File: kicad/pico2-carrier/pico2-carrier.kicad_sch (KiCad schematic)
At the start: 21 parts, among them IC1 TFBS4711-TT1, IC2 M95512-DRMN8TP_K, IC3 IS25WP128F-JBLE, J1 Conn_01x07_Pin, J2 DBG, J3 Ext_Pwr_Rail, SW1 BUT_L, SW2 BUT_M, SW3 BUT_R, U1 Pico 2, U2 BMA400

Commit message: hw: screen updates
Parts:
- J1: symbol Connector:Conn_01x07_Pin -> Connector:Conn_01x08_Pin
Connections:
- net GND: now also J1.8 (Pin_8); no longer J1.7 (Pin_7)
- net ~{SCREEN_RST}: now reaches U1.29 (GPIO22)
- net ~{SCREEN_RST}: now also J1.7 (Pin_7)
- net SCREEN_PWR_EN: now reaches U1.32 (GPIO27_ADC1)
- no-connect marks 9 -> 8
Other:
- note added: "Software reset might be sufficient"
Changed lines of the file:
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@@
 	)
 	(no_connect
-		(at 128.27 135.89)
-	)
-	(no_connect
 		(at 121.92 110.49)
 	)
@@
 	(wire
 		(pts
-			(xy 102.87 76.2) (xy 116.84 76.2)
+			(xy 119.38 128.27) (xy 135.89 128.27)
 		)
 		(stroke
@@
 	(wire
 		(pts
-			(xy 119.38 125.73) (xy 138.43 125.73)
+			(xy 119.38 125.73) (xy 148.59 125.73)
 		)
 		(stroke
@@
 	(wire
 		(pts
+			(xy 102.87 78.74) (xy 116.84 78.74)
+		)
+		(stroke
+			(width 0)
+			(type default)
+		)
+	)
+	(wire
+		(pts
 			(xy 119.38 113.03) (xy 137.16 113.03)
 		)
@@
 	(wire
 		(pts
-			(xy 119.38 135.89) (xy 128.27 135.89)
+			(xy 119.38 135.89) (xy 134.62 135.89)
 		)
 		(stroke
@@
 	(wire
 		(pts
+			(xy 102.87 76.2) (xy 119.38 76.2)
+		)
+		(stroke
+			(width 0)
+			(type default)
+		)
+	)
+	(wire
+		(pts
 			(xy 127 40.64) (xy 127 43.18)
 		)
@@
 		)
 	)
+	(text "Software reset might be sufficient"
+		(exclude_from_sim no)
+		(at 151.892 135.128 0)
+		(effects
+			(font
+				(size 1.27 1.27)
+			)
+		)
+	)
 	(text "1.7V - 5.5V at normal temperatures"
 		(exclude_from_sim no)
@@
 		)
 	)
+	(label "~{SCREEN_RST}"
+		(at 119.38 76.2 180)
+		(fields_autoplaced yes)
+		(effects
+			(font
+				(size 1.27 1.27)
+			)
+			(justify right bottom)
+		)
+	)
 	(label "BUT_R"
 		(at 127 21.59 0)
@@
 		)
 	)
+	(label "~{SCREEN_RST}"
+		(at 134.62 135.89 180)
+		(fields_autoplaced yes)
+		(effects
+			(font
+				(size 1.27 1.27)
+			)
+			(justify right bottom)
+		)
+	)
 	(label "BUT_L"
 		(at 66.04 140.97 0)
@@
 		)
 	)
+	(label "SCREEN_PWR_EN"
+		(at 135.89 128.27 180)
+		(fields_autoplaced yes)
+		(effects
+			(font
+				(size 1.27 1.27)
+			)
+			(justify right bottom)
+		)
+	)
 	(label "~{SCREEN_CSB}"
 		(at 119.38 60.96 180)
@@
 	)
 	(symbol
-		(lib_name "GND_1")
-		(lib_id "power:GND")
-		(at 116.84 76.2 0)
-		(unit 1)
-		(exclude_from_sim no)
-		(in_bom yes)
-		(on_board yes)
-		(dnp no)
-		(fields_autoplaced yes)
-		(property "Reference" "#PWR09"
-			(at 116.84 82.55 0)
-			(effects
-				(font
-					(size 1.27 1.27)
-				)
-				(hide yes)
-			)
-		)
-		(property "Value" "GND"
-			(at 116.84 81.28 0)
-			(effects
-				(font
-					(size 1.27 1.27)
-				)
-			)
-		)
-		(property "Footprint" ""
-			(at 116.84 76.2 0)
-			(effects
-				(font
-					(size 1.27 1.27)
-				)
-				(hide yes)
-			)
-		)
-		(property "Datasheet" ""
-			(at 116.84 76.2 0)
-			(effects
-				(font
-					(size 1.27 1.27)
-				)
-				(hide yes)
-			)
-		)
-		(property "Description" "Power symbol creates a global label with name \"GND\" , ground"
-			(at 116.84 76.2 0)
-			(effects
-				(font
-					(size 1.27 1.27)
-				)
-				(hide yes)
-			)
-		)
-		(pin "1"
-		)
-		(instances
-			(project "pico2-carrier"
-				(path "/4204b4ad-0ae5-4a8a-a079-fb4cf2b0ed9e"
-					(reference "#PWR09")
-					(unit 1)
-				)
-			)
-		)
-	)
-	(symbol
 		(lib_id "power:+3.3V")
 		(at 280.67 52.07 0)
@@
 	)
 	(symbol
-		(lib_id "Connector:Conn_01x07_Pin")
+		(lib_id "Connector:Conn_01x08_Pin")
 		(at 97.79 68.58 0)
 		(unit 1)
@@
 			)
 		)
-		(property "Description" "Generic connector, single row, 01x07, script generated"
+		(property "Description" "Generic connector, single row, 01x08, script generated"
 			(at 97.79 68.58 0)
 			(effects
@@
 		(pin "1"
 		)
+		(pin "8"
+		)
 		(instances
 			(project ""
@@
 		(lib_name "GND_1")
 		(lib_id "power:GND")
-		(at 138.43 125.73 0)
+		(at 148.59 125.73 0)
 		(unit 1)
 		(exclude_from_sim no)
@@
 		(fields_autoplaced yes)
 		(property "Reference" "#PWR027"
-			(at 138.43 132.08 0)
+			(at 148.59 132.08 0)
 			(effects
 				(font
@@
 		)
 		(property "Value" "GND"
-			(at 138.43 130.81 0)
+			(at 148.59 130.81 0)
 			(effects
 				(font
@@
 		)
 		(property "Footprint" ""
-			(at 138.43 125.73 0)
+			(at 148.59 125.73 0)
 			(effects
 				(font
@@
 		)
 		(property "Datasheet" ""
-			(at 138.43 125.73 0)
+			(at 148.59 125.73 0)
 			(effects
 				(font
@@
 		)
 		(property "Description" "Power symbol creates a global label with name \"GND\" , ground"
-			(at 138.43 125.73 0)
+			(at 148.59 125.73 0)
 			(effects
 				(font
@@
 					(unit 1)
 				)
+			)
+		)
+	)
+	(symbol
+		(lib_name "GND_1")
+		(lib_id "power:GND")
+		(at 116.84 78.74 0)
+		(unit 1)
+		(exclude_from_sim no)
+		(in_bom yes)
+		(on_board yes)
+		(dnp no)
+		(fields_autoplaced yes)
+		(property "Reference" "#PWR09"
+			(at 116.84 85.09 0)
+			(effects
+				(font
+					(size 1.27 1.27)
+				)
+				(hide yes)
+			)
+		)
+		(property "Value" "GND"
+			(at 116.84 83.82 0)
+			(effects
+				(font
+					(size 1.27 1.27)
+				)
+			)
+		)
+		(property "Footprint" ""
+			(at 116.84 78.74 0)
+			(effects
+				(font
+					(size 1.27 1.27)
+				)
+				(hide yes)
+			)
+		)
+		(property "Datasheet" ""
+			(at 116.84 78.74 0)
+			(effects
+				(font
+					(size 1.27 1.27)
+				)
+				(hide yes)
+			)
+		)
+		(property "Description" "Power symbol creates a global label with name \"GND\" , ground"
+			(at 116.84 78.74 0)
+			(effects
+				(font
+					(size 1.27 1.27)
+				)
+				(hide yes)
+			)
+		)
+		(pin "1"
+		)
+		(instances
+			(project "pico2-carrier"
+				(path "/4204b4ad-0ae5-4a8a-a079-fb4cf2b0ed9e"
+					(reference "#PWR09")
+					(unit 1)
+				)

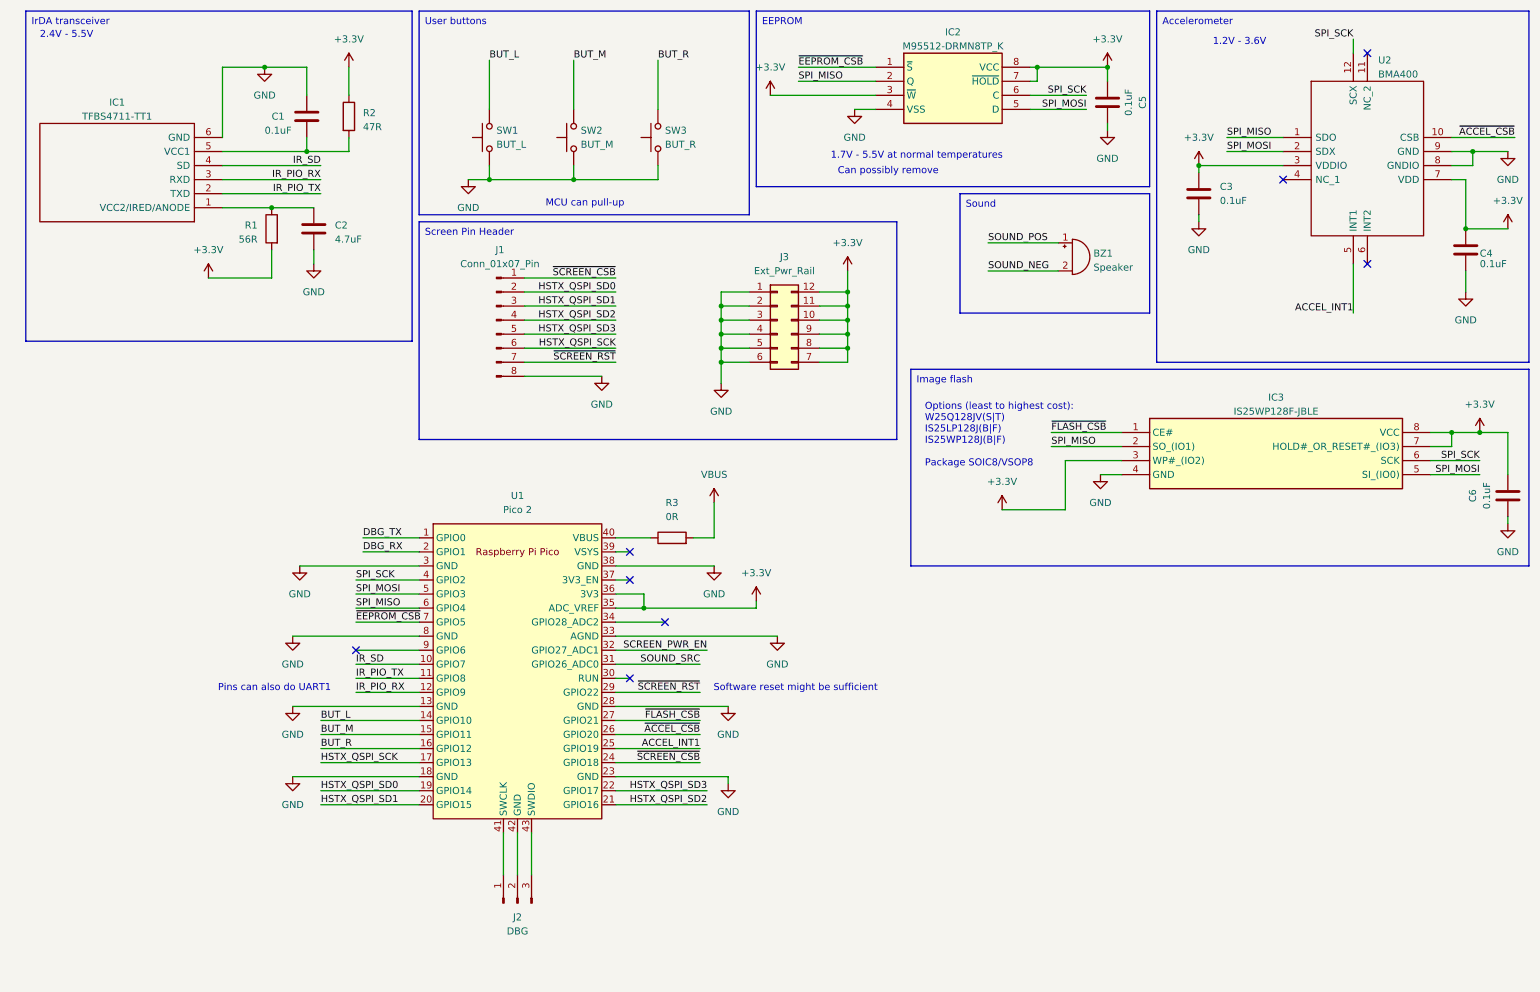
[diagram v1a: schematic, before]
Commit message: hw: update screen stuff
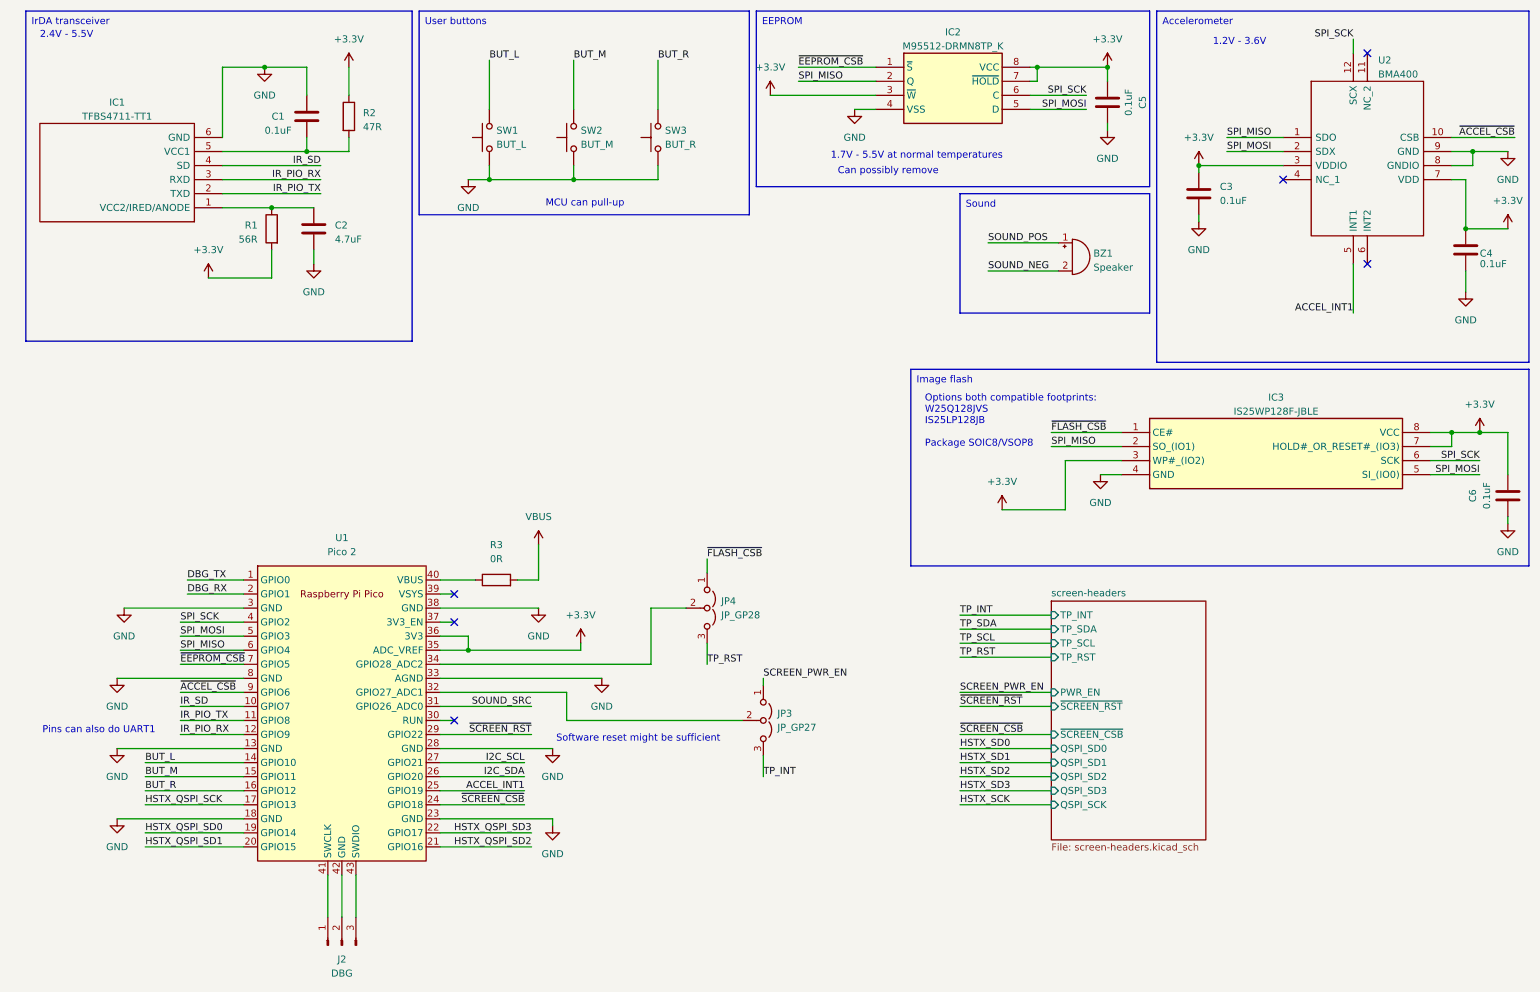
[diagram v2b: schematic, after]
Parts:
- removed J1: Conn_01x07_Pin, symbol Connector:Conn_01x08_Pin
- removed J3: Ext_Pwr_Rail, symbol Connector_Generic:Conn_02x06_Counter_Clockwise
- added JP3: JP_GP27, symbol Jumper:Jumper_3_Open
- added JP4: JP_GP28, symbol Jumper:Jumper_3_Open
- IC1: footprint Samacsys_Parts:TFBS4711TT1 -> SamacsysParts:TFBS4711TT1
- IC2: footprint SOIC127P600X175-8N -> SamacsysParts:SOIC127P600X175-8N
- IC3: footprint SOIC127P790X216-8N -> SamacsysParts:SOIC127P790X216-8N
- J2: footprint (none) -> Connector_PinHeader_2.54mm:PinHeader_1x03_P2.54mm_Vertical
- R3: footprint (none) -> Resistor_SMD:R_0805_2012Metric
- SW1, SW2, SW3: footprint Samacsys_Parts:TL3315NF100Q -> SamacsysParts:TL3315NF100Q
- U2: footprint Samacsys_Parts:BOSCH_LGA-12 -> SamacsysParts:BOSCH_LGA-12
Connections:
- net SCREEN_PWR_EN: now also JP3.1 (A); no longer U1.32 (GPIO27_ADC1)
- net ~{ACCEL_CSB}: now also U1.9 (GPIO6); no longer U1.26 (GPIO20)
- net ~{FLASH_CSB}: now also JP4.1 (A); no longer U1.27 (GPIO21)
- net at U1.34 (GPIO28_ADC2): now also JP4.2 (C)
- new net: JP3.2 (C), U1.32 (GPIO27_ADC1)
- new net I2C_SCL: U1.27 (GPIO21)
- new net I2C_SDA: U1.26 (GPIO20)
- new net TP_INT: JP3.3 (B)
- new net TP_RST: JP4.3 (B)
- no-connect marks 8 -> 6
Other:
- added sheet screen-headers (screen-headers.kicad_sch)
- note added: "Options both compatible footprints: W25Q128JVS IS25LP128JB Package SOIC8/VSOP8"
- note removed: "Options (least to highest cost): W25Q128JV(S|T) IS25LP128J(B|F) IS25WP128J(B|F) Package SOIC8/VSOP8"
- moved on the sheet: J2, R3, U1

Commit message: hw: lots of changes to pico 2 board
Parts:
- removed BZ1: Speaker, Jumper:SolderJumper-2_P1.3mm_Open_Pad1.0x1.5mm, symbol Device:Buzzer
- removed J2: DBG, Connector_PinHeader_2.54mm:PinHeader_1x03_P2.54mm_Vertical, symbol Connector:Conn_01x03_Pin
- removed JP3: JP_GP27, symbol Jumper:Jumper_3_Open
- removed JP4: JP_GP28, symbol Jumper:Jumper_3_Open
- removed R3: 0R, Resistor_SMD:R_0805_2012Metric, symbol Device:R
- removed U2: BMA400, SamacsysParts:BOSCH_LGA-12, symbol SamacSys_Parts:BMA400
- added AC1: BMA400, SamacsysParts:BOSCH_LGA-12, symbol SamacSys_Parts:BMA400
- added H1, H2, H3, H4: MountingHole, MountingHole:MountingHole_2.2mm_M2, symbol Mechanical:MountingHole
- added JP1, JP2: Jumper_2_Open, Connector_PinHeader_2.54mm:PinHeader_1x02_P2.54mm_Vertical, symbol Jumper:Jumper_2_Open
- added JP5: 3V3_CURRENT_SENSE, Connector_PinHeader_2.54mm:PinHeader_1x02_P2.54mm_Vertical, symbol Jumper:Jumper_2_Open
- added R8, R9: 10k, Resistor_SMD:R_0402_1005Metric, symbol Device:R
- added SW4: RUN, Button_Switch_SMD:SW_SPST_Omron_B3FS-101xP, symbol Switch:SW_Push
- SW1, SW2, SW3: footprint SamacsysParts:TL3315NF100Q -> Button_Switch_SMD:SW_SPST_Omron_B3FS-101xP
- renumbered C5 to C3, C3 to C4, C4 to C5
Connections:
- net HSTX_QSPI_SCK is gone; now on net HSTX_SD0: U1.17 (GPIO13)
- net HSTX_QSPI_SD0 is gone; now on net HSTX_SD1: U1.19 (GPIO14)
- net HSTX_QSPI_SD1 is gone; now on net HSTX_SCK: U1.20 (GPIO15)
- net HSTX_QSPI_SD2 is gone; now on net HSTX_SD2: U1.21 (GPIO16)
- net HSTX_QSPI_SD3 is gone; now on net HSTX_SD3: U1.22 (GPIO17)
- net SOUND_SRC is gone; now on net BUT_M: U1.31 (GPIO26_ADC0)
- net +3.3V: now also AC1.3 (VDDIO), AC1.7 (VDD), JP5.2 (B), R8.1, R9.1; no longer U1.35 (ADC_VREF), U1.36 (3V3)
- net ACCEL_INT1: now also U1.10 (GPIO7), AC1.5 (INT1); no longer U1.25 (GPIO19)
- net BUT_L: now also U1.29 (GPIO22); no longer U1.14 (GPIO10)
- net BUT_M: no longer U1.15 (GPIO11)
- net BUT_R: now also U1.32 (GPIO27_ADC1); no longer U1.16 (GPIO12)
- net GND: now also U1.42 (GND), AC1.8 (GNDIO), AC1.9 (GND), SW4.1
- net I2C_SCL: now also R8.2
- net I2C_SDA: now also R9.2
- net IR_PIO_RX: now also U1.14 (GPIO10); no longer U1.12 (GPIO9)
- net IR_PIO_TX: now also U1.15 (GPIO11); no longer U1.11 (GPIO8)
- net IR_SD: now also U1.12 (GPIO9); no longer U1.10 (GPIO7)
- net SPI_MISO: now also AC1.1 (SDO)
- net SPI_MOSI: now also AC1.2 (SDX)
- net SPI_SCK: now also AC1.12 (SCX)
- net VBUS: now also JP1.2 (B)
- net ~{ACCEL_CSB}: now also AC1.10 (CSB)
- net ~{FLASH_CSB}: now also U1.11 (GPIO8)
- net ~{SCREEN_RST}: now also U1.16 (GPIO12); no longer U1.29 (GPIO22)
- net VCC1: now reaches C1.2, IC1.5 (VCC1), R2.2
- net ~{BAT_CE}: now reaches U1.34 (GPIO28_ADC2)
- net VCC2: now reaches C2.1, IC1.1 (VCC2/IRED/ANODE), R1.1
- net SWCLK: now reaches U1.41 (SWCLK)
- net SWDIO: now reaches U1.43 (SWDIO)
- net at U1.40 (VBUS): now also JP1.1 (A)
- net RUN: now reaches U1.30 (RUN)
- net RUN: now also SW4.2
- net at U1.39 (VSYS): now also JP2.1 (A)
- new net: JP5.1 (A), U1.35 (ADC_VREF), U1.36 (3V3)
- new net VSYS: JP2.2 (B)
- new net ~{BAT_INT}: U1.25 (GPIO19)
- no-connect marks 6 -> 4
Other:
- added sheet battery-bq25628e (battery-bq25628e.kicad_sch)
- sheet screen-headers ports: added none; removed PWR_EN, TP_INT, TP_RST, TP_SCL, TP_SDA
- note added: "Candidate: Omron B3FS-1010P"
- note added: "Pins on pico"
- note added: "Removed sound because lack of pins"
- note added: "Weird HSTX pins placement for better routing Can easily reconfigure in software"
